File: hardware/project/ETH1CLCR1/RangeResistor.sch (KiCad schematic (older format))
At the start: 95 parts, among them K1201 TQ2SA-5V, Q1201 BC847W, Q1202 2N2218A, Q1203 2N2904A, Q1204 BC847W, U1201 TL072, U1202 AD5293BRUZ-20, U1203 AQY212GS, U1204 HA3-2525-5Z, U1205 AQY212GS, U1206 AQY212GS, U1207 AQY212GS, U1208 AQY212GS, U1209 AQY212GS, U1210 AQY212GS, U1211 AQY212GS, U1212 AQY212GS, U1213 AQY212GS, U1214 AQY212GS, U1215 AQY212GS

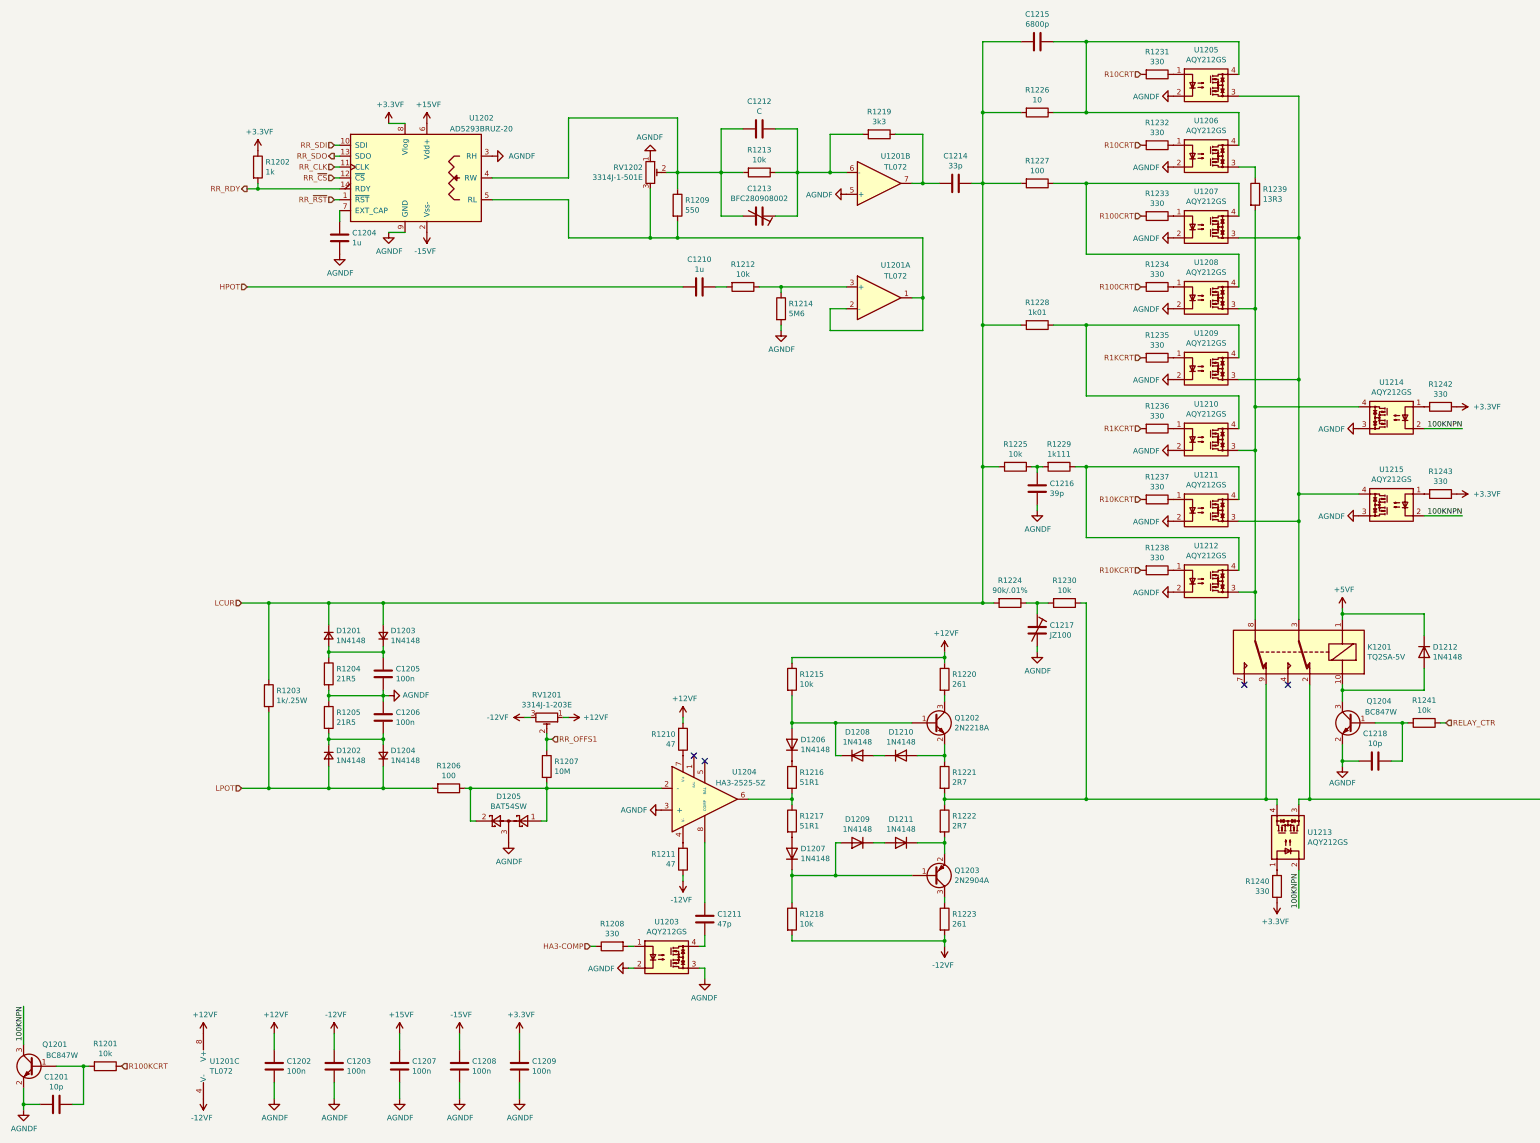
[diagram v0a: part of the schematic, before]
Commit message: Redesigned the power supply, added humidy+temp. sensor.
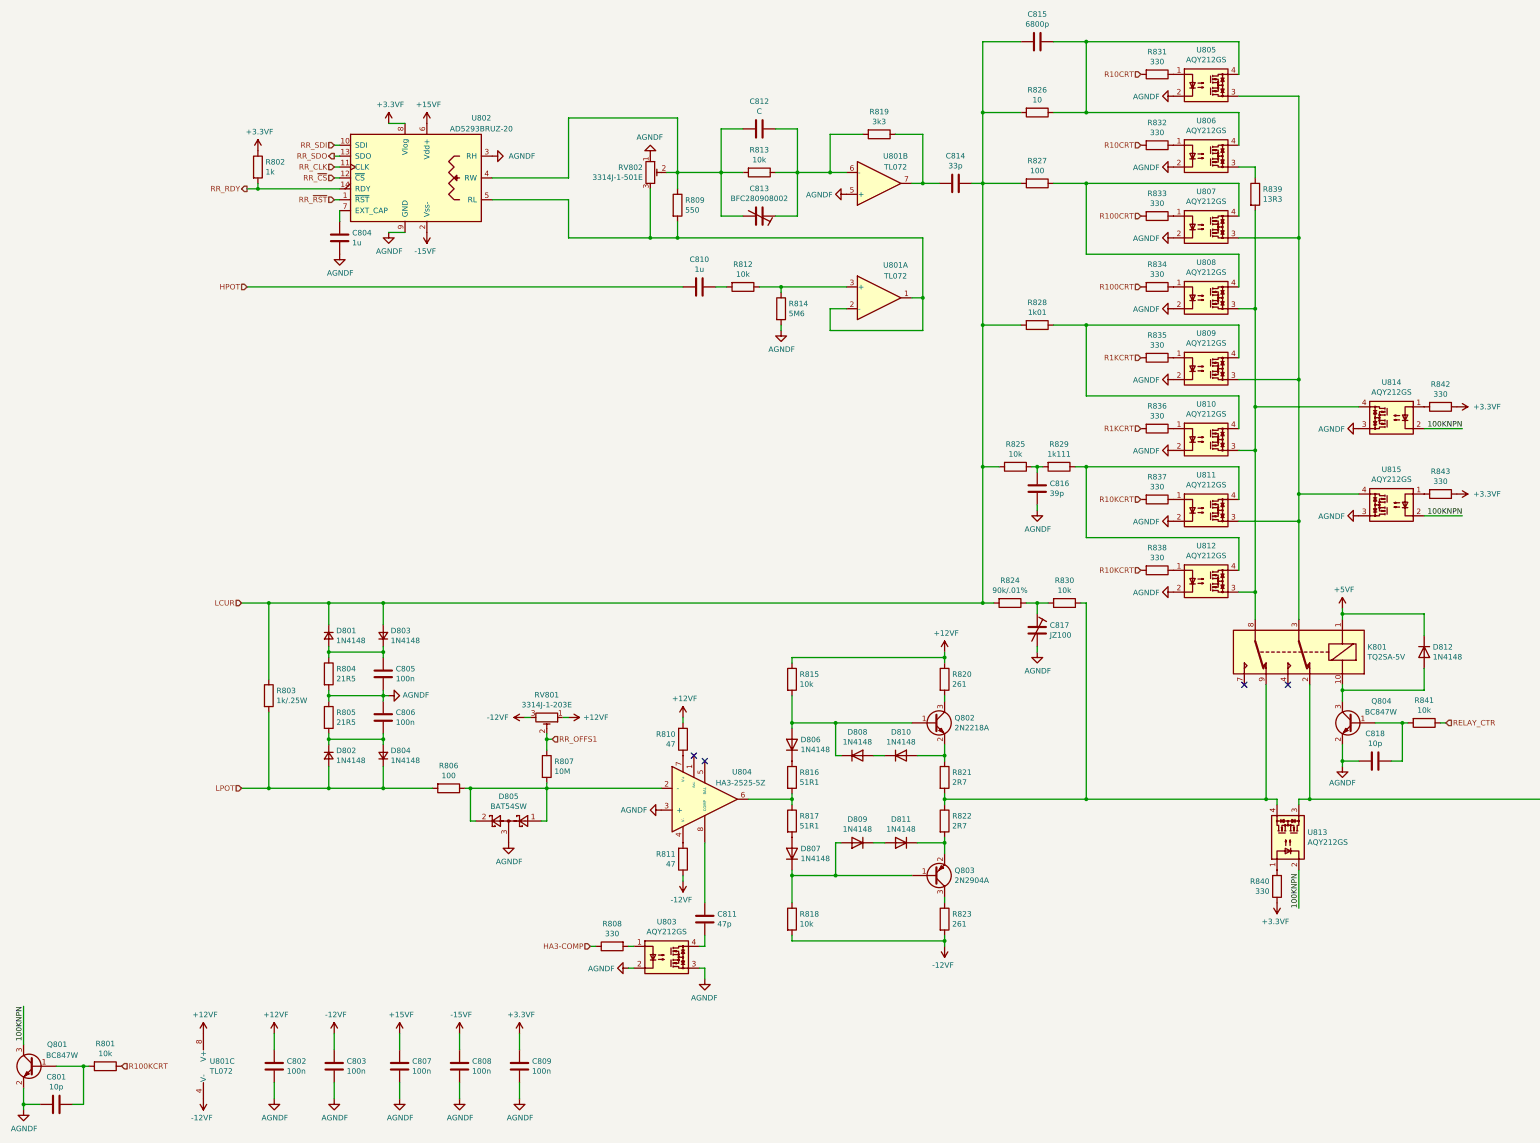
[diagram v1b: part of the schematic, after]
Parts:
- renumbered C1201 to C801, C1202 to C802, C1203 to C803, C1204 to C804, C1205 to C805, C1206 to C806, C1207 to C807, C1208 to C808, C1209 to C809, C1210 to C810, C1211 to C811, C1212 to C812, C1213 to C813, C1214 to C814, C1215 to C815, C1216 to C816, C1217 to C817, C1218 to C818, D1201 to D801, D1202 to D802, D1203 to D803, D1204 to D804, D1205 to D805, D1206 to D806, D1207 to D807, D1208 to D808, D1209 to D809, D1210 to D810, D1211 to D811, D1212 to D812, K1201 to K801, Q1201 to Q801, Q1202 to Q802, Q1203 to Q803, Q1204 to Q804, R1201 to R801, R1202 to R802, R1203 to R803, R1204 to R804, R1205 to R805, R1206 to R806, R1207 to R807, R1208 to R808, R1209 to R809, R1210 to R810, R1211 to R811, R1212 to R812, R1213 to R813, R1214 to R814, R1215 to R815, R1216 to R816, R1217 to R817, R1218 to R818, R1219 to R819, R1220 to R820, R1221 to R821, R1222 to R822, R1223 to R823, R1224 to R824, R1225 to R825, R1226 to R826, R1227 to R827, R1228 to R828, R1229 to R829, R1230 to R830, R1231 to R831, R1232 to R832, R1233 to R833, R1234 to R834, R1235 to R835, R1236 to R836, R1237 to R837, R1238 to R838, R1239 to R839, R1240 to R840, R1241 to R841, R1242 to R842, R1243 to R843, RV1201 to RV801, RV1202 to RV802, U1201 to U801, U1202 to U802, U1203 to U803, U1204 to U804, U1205 to U805, U1206 to U806, U1207 to U807, U1208 to U808, U1209 to U809, U1210 to U810, U1211 to U811, U1212 to U812, U1213 to U813, U1214 to U814, U1215 to U815

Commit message: PCB layout
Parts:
- R804, R805: value 21R5 -> 21R5/.5W; footprint Resistor_SMD:R_0603_1608Metric_Pad1.05x0.95mm_HandSolder -> Resistor_SMD:R_0805_2012Metric_Pad1.15x1.40mm_HandSolder
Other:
- moved on the sheet: D801, D802, R803, R804, R805
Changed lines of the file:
@@
 $EndComp
 Connection ~ 4050 7950
-Connection ~ 3550 7950
-Wire Wire Line
-	3000 7250 3000 7950
-Connection ~ 3550 6250
+Wire Wire Line
+	2900 7250 2900 7950
 Wire Wire Line
 	4100 7100 4050 7100
@@
 	0    -1   -1   0
 $EndComp
-Connection ~ 4050 7500
-Wire Wire Line
-	4050 7550 4050 7500
-Wire Wire Line
-	3550 7950 4050 7950
-Wire Wire Line
-	3550 7500 3550 7550
+Wire Wire Line
+	3450 7500 3450 7550
 $Comp
 L Device:D_Small D804
@@
 L Device:D_Small D802
 U 1 1 5E263E00
-P 3550 7650
-F 0 "D802" V 3504 7718 50  0000 L CNN
-F 1 "1N4148" V 3595 7718 50  0000 L CNN
-F 2 "Diode_SMD:D_SOD-123" V 3550 7650 50  0001 C CNN
-F 3 "~" V 3550 7650 50  0001 C CNN
-	1    3550 7650
-	0    1    1    0
-$EndComp
-Connection ~ 4050 6700
-Wire Wire Line
-	4050 6650 4050 6700
-Wire Wire Line
-	3550 6250 4050 6250
-Wire Wire Line
-	3550 6700 3550 6650
+P 3450 7650
+F 0 "D802" V 3404 7718 50  0000 L CNN
+F 1 "1N4148" V 3495 7718 50  0000 L CNN
+F 2 "Diode_SMD:D_SOD-123" V 3450 7650 50  0001 C CNN
+F 3 "~" V 3450 7650 50  0001 C CNN
+	1    3450 7650
+	0    1    1    0
+$EndComp
+Wire Wire Line
+	3450 6700 3450 6650
 $Comp
 L Device:D_Small D803
@@
 $EndComp
 Wire Wire Line
-	3550 7100 4050 7100
+	3450 7100 4050 7100
 Wire Wire Line
 	4050 7100 4050 7050
@@
 Connection ~ 4050 7100
 Wire Wire Line
-	3550 7150 3550 7100
-Wire Wire Line
-	3550 7100 3550 7050
-Connection ~ 3550 7100
-Wire Wire Line
-	4050 6700 4050 6750
-Wire Wire Line
-	4050 7500 4050 7450
-Wire Wire Line
-	3550 7500 4050 7500
-Wire Wire Line
-	3550 6700 4050 6700
+	3450 7150 3450 7100
+Wire Wire Line
+	3450 7100 3450 7050
+Connection ~ 3450 7100
+Wire Wire Line
+	3450 7500 4050 7500
+Wire Wire Line
+	3450 6700 4050 6700
 $Comp
 L Device:D_Small D801
 U 1 1 5E25D927
-P 3550 6550
-F 0 "D801" V 3504 6618 50  0000 L CNN
-F 1 "1N4148" V 3595 6618 50  0000 L CNN
-F 2 "Diode_SMD:D_SOD-123" V 3550 6550 50  0001 C CNN
-F 3 "~" V 3550 6550 50  0001 C CNN
-	1    3550 6550
-	0    1    1    0
-$EndComp
-Connection ~ 3550 6700
-Connection ~ 3550 7500
-Wire Wire Line
-	3550 7450 3550 7500
-Wire Wire Line
-	3550 6750 3550 6700
-$Comp
-L Device:R R805
-U 1 1 5E258709
-P 3550 7300
-F 0 "R805" H 3620 7346 50  0000 L CNN
-F 1 "21R5" H 3620 7255 50  0000 L CNN
-F 2 "Resistor_SMD:R_0603_1608Metric_Pad1.05x0.95mm_HandSolder" V 3480 7300 50  0001 C CNN
-F 3 "~" H 3550 7300 50  0001 C CNN
-	1    3550 7300
-	1    0    0    -1
-$EndComp
+P 3450 6550
+F 0 "D801" V 3404 6618 50  0000 L CNN
+F 1 "1N4148" V 3495 6618 50  0000 L CNN
+F 2 "Diode_SMD:D_SOD-123" V 3450 6550 50  0001 C CNN
+F 3 "~" V 3450 6550 50  0001 C CNN
+	1    3450 6550
+	0    1    1    0
+$EndComp
+Connection ~ 3450 6700
+Connection ~ 3450 7500
+Wire Wire Line
+	3450 7450 3450 7500
+Wire Wire Line
+	3450 6750 3450 6700
 $Comp
 L Device:R R804
 U 1 1 5E256242
-P 3550 6900
-F 0 "R804" H 3620 6946 50  0000 L CNN
-F 1 "21R5" H 3620 6855 50  0000 L CNN
-F 2 "Resistor_SMD:R_0603_1608Metric_Pad1.05x0.95mm_HandSolder" V 3480 6900 50  0001 C CNN
-F 3 "~" H 3550 6900 50  0001 C CNN
-	1    3550 6900
+P 3450 6900
+F 0 "R804" H 3520 6946 50  0000 L CNN
+F 1 "21R5/.5W" H 3520 6855 50  0000 L CNN
+F 2 "Resistor_SMD:R_0805_2012Metric_Pad1.15x1.40mm_HandSolder" V 3380 6900 50  0001 C CNN
+F 3 "~" H 3450 6900 50  0001 C CNN
+	1    3450 6900
 	1    0    0    -1
 $EndComp
@@
 L Device:R R803
 U 1 1 5E254517
-P 3000 7100
-F 0 "R803" H 3070 7146 50  0000 L CNN
-F 1 "1k/.25W" H 3070 7055 50  0000 L CNN
-F 2 "Resistor_SMD:R_1206_3216Metric_Pad1.42x1.75mm_HandSolder" V 2930 7100 50  0001 C CNN
-F 3 "~" H 3000 7100 50  0001 C CNN
-	1    3000 7100
+P 2900 7100
+F 0 "R803" H 2970 7146 50  0000 L CNN
+F 1 "1k/.25W" H 2970 7055 50  0000 L CNN
+F 2 "Resistor_SMD:R_1206_3216Metric_Pad1.42x1.75mm_HandSolder" V 2830 7100 50  0001 C CNN
+F 3 "~" H 2900 7100 50  0001 C CNN
+	1    2900 7100
 	1    0    0    -1
 $EndComp
@@
 	1    0    0    -1
 $EndComp
-Connection ~ 3000 6250
-Wire Wire Line
-	3000 6250 2750 6250
-Connection ~ 3000 7950
-Wire Wire Line
-	3000 7950 2750 7950
-Wire Wire Line
-	3000 7950 3550 7950
-Wire Wire Line
-	3000 6250 3550 6250
 Connection ~ 4050 6250
 Wire Wire Line
@@
 	4050 7750 4050 7950
 Wire Wire Line
-	3550 7750 3550 7950
-Wire Wire Line
-	3000 6250 3000 6950
-Wire Wire Line
-	3550 6250 3550 6450
+	3450 7750 3450 7950
+Wire Wire Line
+	2900 6250 2900 6950
+Wire Wire Line
+	3450 6250 3450 6450
 $Comp
 L ETH1CLCR1:-12VF #PWR0823
@@
 Wire Wire Line
 	9650 6250 9550 6250
+Wire Wire Line
+	4050 7450 4050 7500
+Wire Wire Line
+	4050 6650 4050 6700
+Connection ~ 3450 6250
+Connection ~ 3450 7950
+Wire Wire Line
+	3450 7950 4050 7950
+Wire Wire Line
+	3450 6250 4050 6250
+Connection ~ 4050 6700
+Wire Wire Line
+	4050 6700 4050 6750
+Connection ~ 4050 7500
+Wire Wire Line
+	4050 7500 4050 7550
+$Comp
+L Device:R R805
+U 1 1 5E258709
+P 3450 7300
+F 0 "R805" H 3520 7346 50  0000 L CNN
+F 1 "21R5/.5W" H 3520 7255 50  0000 L CNN
+F 2 "Resistor_SMD:R_0805_2012Metric_Pad1.15x1.40mm_HandSolder" V 3380 7300 50  0001 C CNN
+F 3 "~" H 3450 7300 50  0001 C CNN
+	1    3450 7300
+	1    0    0    -1
+$EndComp
+Connection ~ 2900 6250
+Wire Wire Line
+	2900 6250 2750 6250
+Connection ~ 2900 7950
+Wire Wire Line
+	2900 7950 2750 7950
+Wire Wire Line
+	2900 6250 3450 6250
+Wire Wire Line
+	2900 7950 3450 7950
 $EndSCHEMATC

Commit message: Changes in schematics.
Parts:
- added C819, C820, C821, C822: 10p, Capacitor_SMD:C_0603_1608Metric_Pad1.05x0.95mm_HandSolder, symbol Device:C
- added Q805, Q806, Q807, Q808: BC847W, Package_TO_SOT_SMD:SOT-323_SC-70, symbol Transistor_BJT:BC847W
- added R844, R845, R846, R847: 10k, Resistor_SMD:R_0603_1608Metric_Pad1.05x0.95mm_HandSolder, symbol Device:R
- C810: value 1u -> 1u/150V; footprint Capacitor_SMD:C_0603_1608Metric_Pad1.05x0.95mm_HandSolder -> Capacitor_SMD:C_1812_4532Metric_Pad1.30x3.40mm_HandSolder
- C814: value 33p -> 33p/300V
- C815: value 6800p -> 6800p/200V
- R820, R823: value 261 -> 261/.5W; footprint Resistor_SMD:R_0603_1608Metric_Pad1.05x0.95mm_HandSolder -> Resistor_SMD:R_0805_2012Metric_Pad1.15x1.40mm_HandSolder
- R821, R822: value 2R7 -> 2R7/.5W
- R824: value 90k/.01% -> RN732BTTD9002B25; footprint Resistor_SMD:R_0603_1608Metric_Pad1.05x0.95mm_HandSolder -> Resistor_SMD:R_1206_3216Metric_Pad1.42x1.75mm_HandSolder
- R825, R830: value 10k -> RN732ATTE1002B25
- R826: value 10 -> RP73PF2A10RBTDF; footprint Resistor_SMD:R_0603_1608Metric_Pad1.05x0.95mm_HandSolder -> Resistor_SMD:R_0805_2012Metric_Pad1.15x1.40mm_HandSolder
- R827: value 100 -> RT1206BRB07100RL; footprint Resistor_SMD:R_0603_1608Metric_Pad1.05x0.95mm_HandSolder -> Resistor_SMD:R_1206_3216Metric_Pad1.42x1.75mm_HandSolder
- R828: value 1k01 -> TNPW08051K01BEEA; footprint Resistor_SMD:R_0603_1608Metric_Pad1.05x0.95mm_HandSolder -> Resistor_SMD:R_0805_2012Metric_Pad1.15x1.40mm_HandSolder
- R829: value 1k111 -> RN73R2BTTD1001B25; footprint Resistor_SMD:R_0603_1608Metric_Pad1.05x0.95mm_HandSolder -> Resistor_SMD:R_1206_3216Metric_Pad1.42x1.75mm_HandSolder
- R831, R832, R833, R834, R835, R836, R837, R838: value 330 -> 680
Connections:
- net +5VF: now also R831.2, R832.2, R833.2, R834.2, R835.2, R836.2, R837.2, R838.2
- net AGNDF: now also C819.2, C820.2, C821.2, C822.2, Q805.2 (E), Q806.2 (E), Q807.2 (E), Q808.2 (E); no longer U805.2, U806.2, U807.2, U808.2, U809.2, U810.2, U811.2, U812.2
- net R100CRT: now also R846.1; no longer R833.2, R834.2
- net R10CRT: now also R844.1; no longer R831.2, R832.2
- net R10KCRT: now also R847.1; no longer R837.2, R838.2
- net R1KCRT: now also R845.1; no longer R835.2, R836.2
- new net: C819.1, Q805.1 (B), R844.2
- new net: C821.1, Q807.1 (B), R846.2
- new net: C820.1, Q806.1 (B), R845.2
- new net: C822.1, Q808.1 (B), R847.2
- new net R100NPN: Q807.3 (C), U807.2, U808.2
- new net R10KNPN: Q808.3 (C), U811.2, U812.2
- new net R10NPN: Q805.3 (C), U805.2, U806.2
- new net R1KNPN: Q806.3 (C), U809.2, U810.2
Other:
- note added: "10"
- note added: "100"
- note added: "10k"
- note added: "1k"
- note added: "1k01"
- note added: "90k"
- moved on the sheet: C801, C804, C805, C806, C810, C811, C812, C813, C814, C815, C816, C817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

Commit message: Checked the schematics. Created BOM.
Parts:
- C810: value 1u/150V -> 1u/100V
- C814: value 33p/300V -> 33p/200V
- R802: value 1k -> 2k2
- R824: value RN732BTTD9002B25 -> 90k
- R825, R830: value RN732ATTE1002B25 -> 10k
- R826: value RP73PF2A10RBTDF -> 10
- R827: value RT1206BRB07100RL -> 100
- R828: value TNPW08051K01BEEA -> 1k01
- R829: value RN73R2BTTD1001B25 -> 1k
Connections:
- net HA3-COMP renamed RR_HA3-COMP
- net R100CRT renamed RR_100CRT
- net R100KCRT renamed RR_100KCRT
- net R10CRT renamed RR_10CRT
- net R10KCRT renamed RR_10KCRT
- net R1KCRT renamed RR_1KCRT
- net RELAY_CTR renamed RR_RELAYCTR
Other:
- note added: "RN732ATTE1002B25"
- note added: "RN732BTTD9002B25"
- note added: "RN73R2BTTD1001B25"
- note added: "RP73PF2A10RBTDF"
- note added: "RT1206BRB07100RL"
- note added: "TNPW08051K01BEEA"
- note removed: "10"
- note removed: "100"
- note removed: "10k"
- note removed: "1k"
- note removed: "1k01"
- note removed: "90k"
- moved on the sheet: C802, C803, C807, C808, C809, U801C
